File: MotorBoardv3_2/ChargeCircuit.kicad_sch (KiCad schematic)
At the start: 14 parts, among them J20 Barrel_Jack, Q1 TIP42A, U7 MAX712CSE

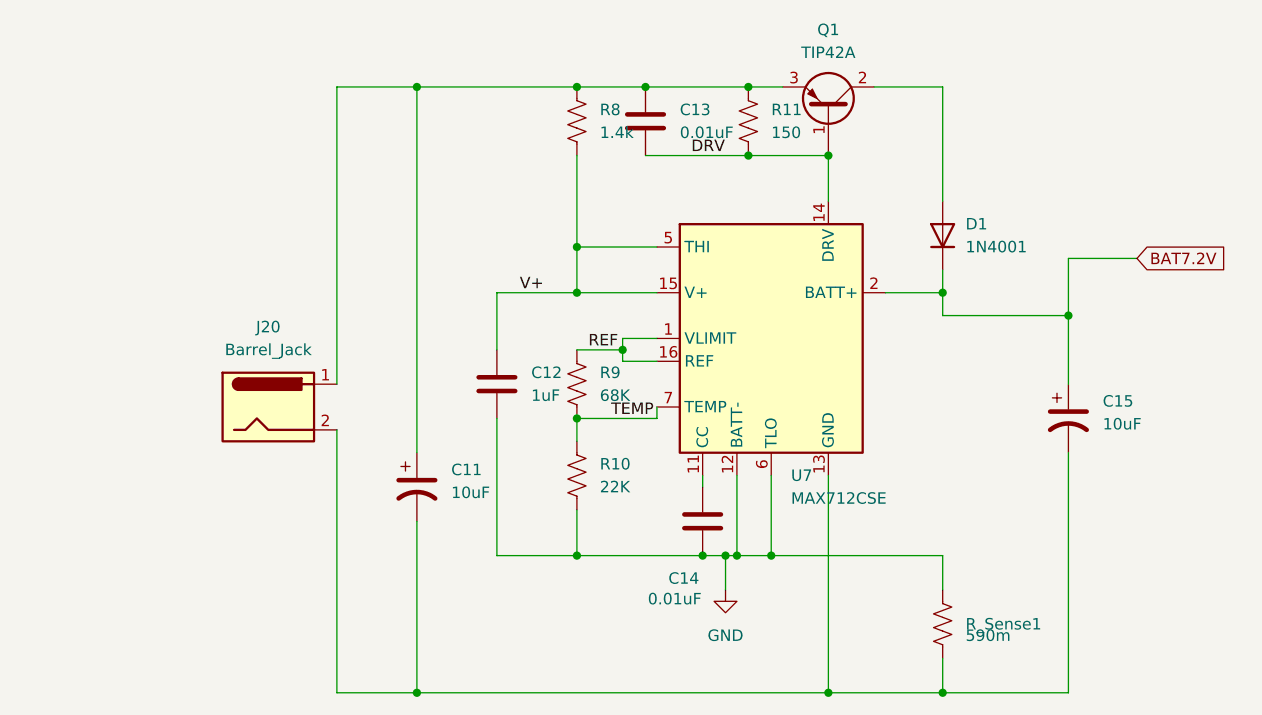
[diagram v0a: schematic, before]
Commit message: Added test points to Charge Circuit
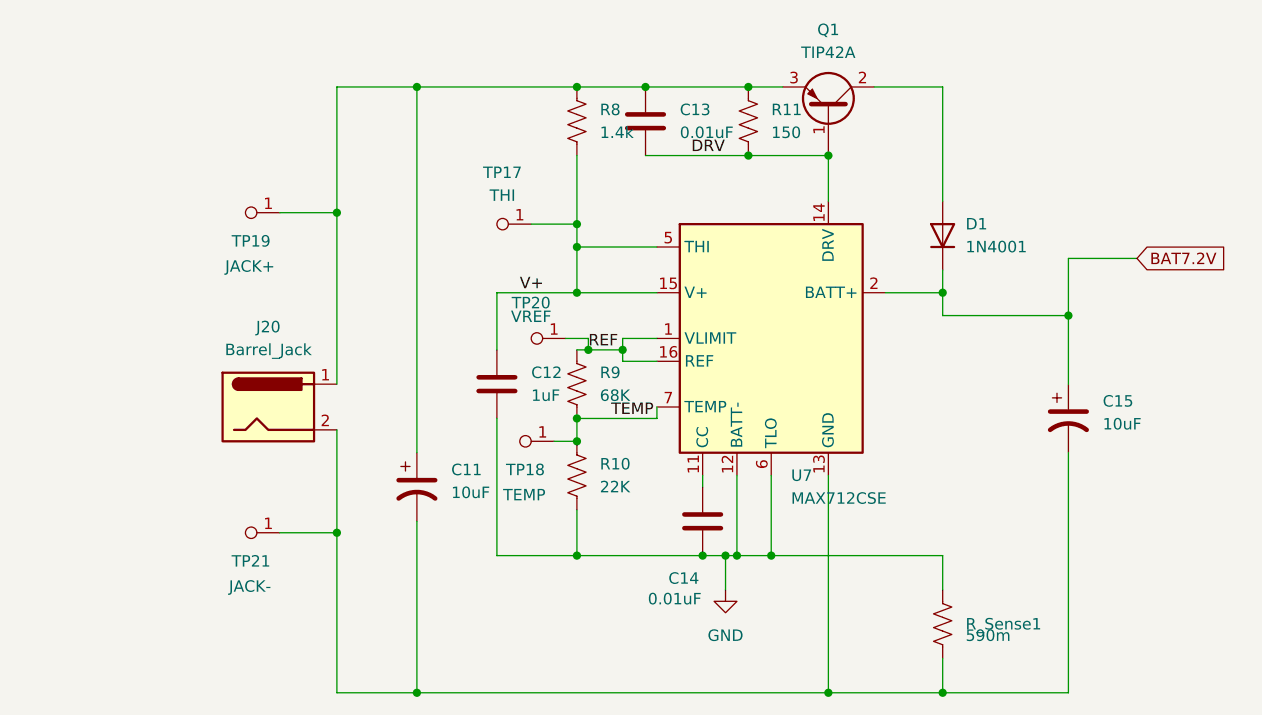
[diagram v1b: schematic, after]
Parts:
- added TP17: THI, RSLK2:Testpoint_1x1, symbol RSLK2:Testpoint_1
- added TP18: TEMP, RSLK2:Testpoint_1x1, symbol RSLK2:Testpoint_1
- added TP19: JACK+, RSLK2:Testpoint_1x1, symbol RSLK2:Testpoint_1
- added TP20: VREF, RSLK2:Testpoint_1x1, symbol RSLK2:Testpoint_1
- added TP21: JACK-, RSLK2:Testpoint_1x1, symbol RSLK2:Testpoint_1
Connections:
- net REF: now also TP20.1 (A)
- net TEMP: now also TP18.1 (A)
- net V+: now also TP17.1 (A)
- net at C11.1, C13.1, J20.1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: now also TP19.1 (A)
- net at C11.2, C15.2, J20.2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: now also TP21.1 (A)

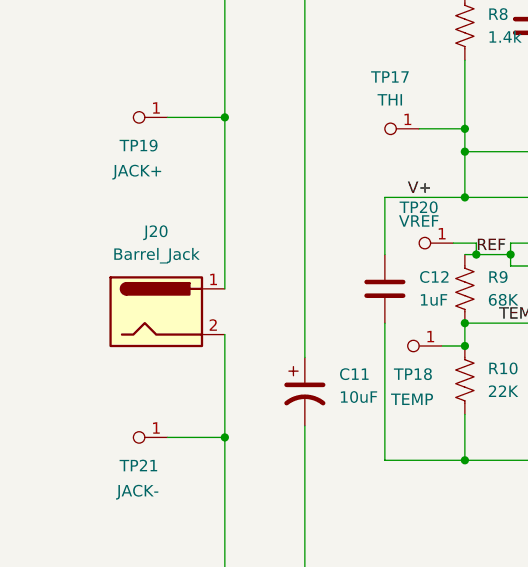
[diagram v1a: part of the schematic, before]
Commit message: Changed Barrel Jack Footprint to incorporate through-hole connections
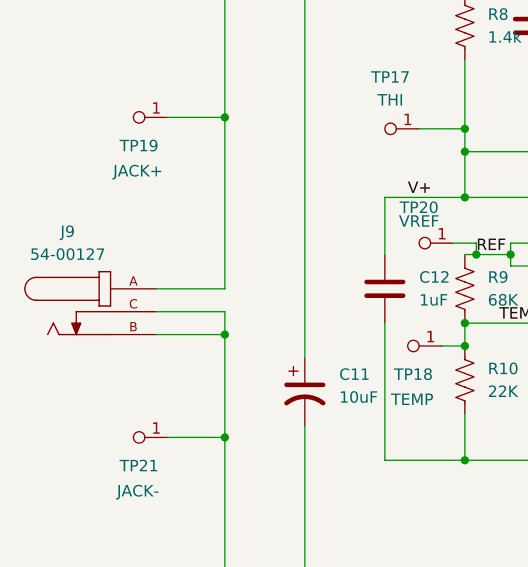
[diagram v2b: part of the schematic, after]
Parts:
- removed J20: Barrel_Jack, RSLK2:54-00127_TEN, symbol Connector:Barrel_Jack
- added J9: 54-00127, RSLK2:TENSILITY_54-00127, symbol RSLK2:54-00127
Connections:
- net at C11.1, C13.1, Q1.3 (E)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: now also J9.A
- net at C11.2, C15.2, R_Sense1.2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: now also J9.B, J9.C
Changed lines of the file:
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@@
+	)
+	(junction
+		(at 95.25 80.01)
+		(diameter 0)
+		(color 0 0 0 0)
 	)
 	(junction
@@
 	(wire
 		(pts
+			(xy 87.63 80.01) (xy 95.25 80.01)
+		)
+		(stroke
+			(width 0)
+			(type default)
+		)
+	)
+	(wire
+		(pts
 			(xy 95.25 109.22) (xy 104.14 109.22)
 		)
@@
 	(wire
 		(pts
+			(xy 87.63 74.93) (xy 95.25 74.93)
+		)
+		(stroke
+			(width 0)
+			(type default)
+		)
+	)
+	(wire
+		(pts
 			(xy 149.86 109.22) (xy 162.56 109.22)
 		)
@@
 	(wire
 		(pts
+			(xy 87.63 77.47) (xy 95.25 77.47)
+		)
+		(stroke
+			(width 0)
+			(type default)
+		)
+	)
+	(wire
+		(pts
 			(xy 121.92 78.74) (xy 130.81 78.74)
 		)
@@
 		(pts
 			(xy 129.54 41.91) (xy 140.97 41.91)
+		)
+		(stroke
+			(width 0)
+			(type default)
+		)
+	)
+	(wire
+		(pts
+			(xy 95.25 77.47) (xy 95.25 80.01)
 		)
 		(stroke
@@
 	)
 	(symbol
+		(lib_id "RSLK2:54-00127")
+		(at 82.55 77.47 0)
+		(unit 1)
+		(exclude_from_sim no)
+		(in_bom yes)
+		(on_board yes)
+		(dnp no)
+		(fields_autoplaced yes)
+		(property "Reference" "J9"
+			(at 77.7903 68.58 0)
+			(effects
+				(font
+					(size 1.27 1.27)
+				)
+			)
+		)
+		(property "Value" "54-00127"
+			(at 77.7903 71.12 0)
+			(effects
+				(font
+					(size 1.27 1.27)
+				)
+			)
+		)
+		(property "Footprint" "RSLK2:TENSILITY_54-00127"
+			(at 82.55 77.47 0)
+			(effects
+				(font
+					(size 1.27 1.27)
+				)
+				(justify bottom)
+				(hide yes)
+			)
+		)
+		(property "Datasheet" ""
+			(at 82.55 77.47 0)
+			(effects
+				(font
+					(size 1.27 1.27)
+				)
+				(hide yes)
+			)
+		)
+		(property "Description" ""
+			(at 82.55 77.47 0)
+			(effects
+				(font
+					(size 1.27 1.27)
+				)
+				(hide yes)
+			)
+		)
+		(property "PARTREV" "A"
+			(at 82.55 77.47 0)
+			(effects
+				(font
+					(size 1.27 1.27)
+				)
+				(justify bottom)
+				(hide yes)
+			)
+		)
+		(property "STANDARD" "Manufacturer Recommendations"
+			(at 82.55 77.47 0)
+			(effects
+				(font
+					(size 1.27 1.27)
+				)
+				(justify bottom)
+				(hide yes)
+			)
+		)
+		(property "SNAPEDA_PN" "54-00127"
+			(at 82.55 77.47 0)
+			(effects
+				(font
+					(size 1.27 1.27)
+				)
+				(justify bottom)
+				(hide yes)
+			)
+		)
+		(property "MAXIMUM_PACKAGE_HEIGHT" "7.3mm"
+			(at 82.55 77.47 0)
+			(effects
+				(font
+					(size 1.27 1.27)
+				)
+				(justify bottom)
+				(hide yes)
+			)
+		)
+		(property "MANUFACTURER" "TENSILITY"
+			(at 82.55 77.47 0)
+			(effects
+				(font
+					(size 1.27 1.27)
+				)
+				(justify bottom)
+				(hide yes)
+			)
+		)
+		(pin "C"
+		)
+		(pin "B"
+		)
+		(pin "A"
+		)
+		(instances
+			(project ""
+				(path "/69b823fd-c065-40ff-9bb9-c5835555f3eb/c3070603-99fb-449f-960f-a7ad5e65d177"
+					(reference "J9")
+					(unit 1)
+				)
+			)
+		)
+	)
+	(symbol
 		(lib_id "RSLK2:Testpoint_1")
 		(at 88.9 89.535 90)
@@
 					(unit 1)
 				)
-			)
-		)
-	)
-	(symbol
-		(lib_id "Connector:Barrel_Jack")
-		(at 87.63 77.47 0)
-		(unit 1)
-		(exclude_from_sim no)
-		(in_bom yes)
-		(on_board yes)
-		(dnp no)
-		(property "Reference" "J20"
-			(at 87.63 68.58 0)
-			(effects
-				(font
-					(size 1.27 1.27)
-				)
-			)
-		)
-		(property "Value" "Barrel_Jack"
-			(at 87.63 71.12 0)
-			(effects
-				(font
-					(size 1.27 1.27)
-				)
-			)
-		)
-		(property "Footprint" "RSLK2:54-00127_TEN"
-			(at 88.9 78.486 0)
-			(effects
-				(font
-					(size 1.27 1.27)
-				)
-				(hide yes)
-			)
-		)
-		(property "Datasheet" "~"
-			(at 88.9 78.486 0)
-			(effects
-				(font
-					(size 1.27 1.27)
-				)
-				(hide yes)
-			)
-		)
-		(property "Description" "DC Barrel Jack"
-			(at 87.63 77.47 0)
-			(effects
-				(font
-					(size 1.27 1.27)
-				)
-				(hide yes)
-			)
-		)
-		(pin "1"
-		)
-		(pin "2"
-		)
-		(instances
-			(project "MotorBoardv3_2"
-				(path "/69b823fd-c065-40ff-9bb9-c5835555f3eb/c3070603-99fb-449f-960f-a7ad5e65d177"
-					(reference "J20")
-					(unit 1)
-				)

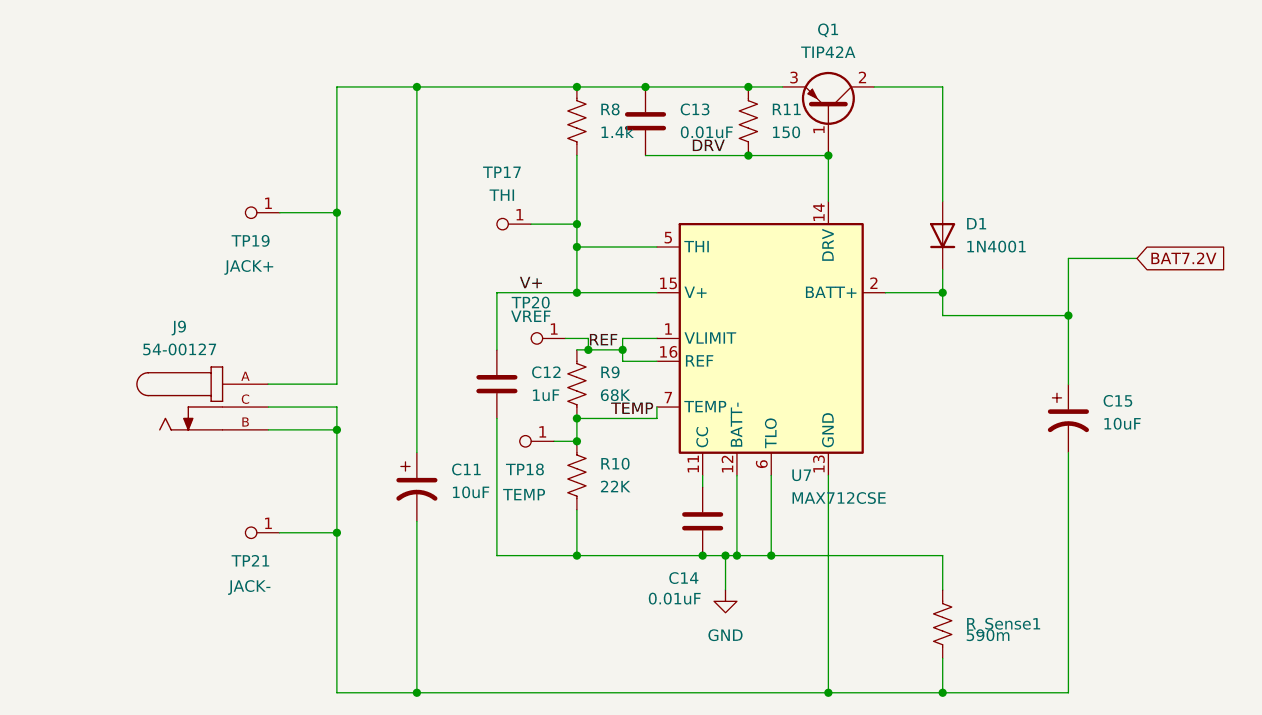
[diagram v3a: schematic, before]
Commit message: added charging indicator led
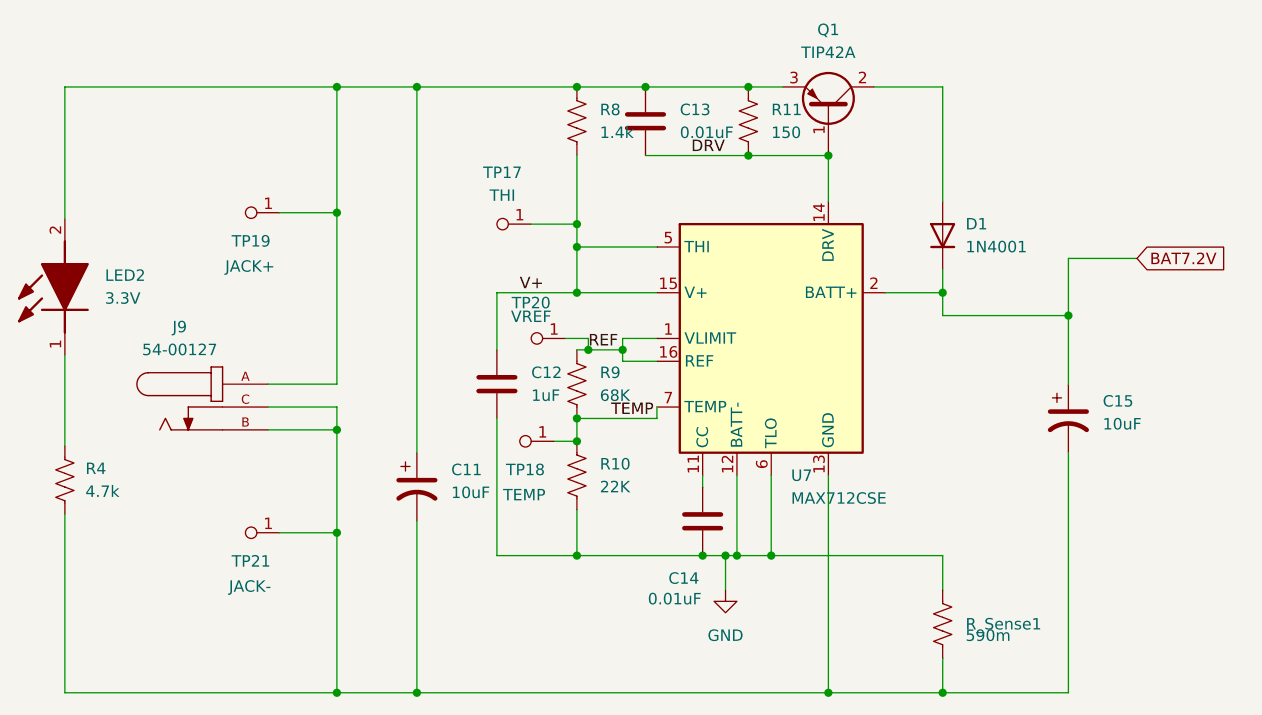
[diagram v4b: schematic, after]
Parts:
- added LED2: 3.3V, RSLK2:APT1608CGCK, symbol RSLK2:APTD1608LSECK_J3-PF
- added R4: 4.7k, RSLK2:R_0603_1608Metric, symbol Device:R_US
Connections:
- net at C11.1, C13.1, J9.A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: now also LED2.2 (A)
- net at C11.2, C15.2, J9.B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: now also R4.2
- new net: LED2.1 (K), R4.1
